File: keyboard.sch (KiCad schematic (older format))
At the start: 37 parts, among them J1 USB_C_Receptacle_USB2.0, J2 -, J3 -, K1 Jumper_NO_Small, P1 SWD, P2 BATT, U1 nRF52810-ND04C, U2 CH554T, U3 TP4057, U4 XC6206P30

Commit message: 更换type-c接口的封装
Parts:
- J1: footprint Connector_USB:USB_C_Receptacle_Amphenol_12401610E4-2A -> Customv2:USB_C_SIMPLE_ONBOARD
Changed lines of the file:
@@
 F 0 "J1" H 1355 6467 50  0000 C CNN
 F 1 "USB_C_Receptacle_USB2.0" H 1355 6376 50  0000 C CNN
-F 2 "Connector_USB:USB_C_Receptacle_Amphenol_12401610E4-2A" H 1400 5600 50  0001 C CNN
+F 2 "Customv2:USB_C_SIMPLE_ONBOARD" H 1400 5600 50  0001 C CNN
 F 3 "https://www.usb.org/sites/default/files/documents/usb_type-c.zip" H 1400 5600 50  0001 C CNN
 	1    1250 5600

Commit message: 增加电容，更改type-c封装为非沉板式
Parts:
- added C9: 1uF, Capacitor_SMD:C_0805_2012Metric, symbol Device:C_Small
- J1: footprint Customv2:USB_C_SIMPLE_ONBOARD -> Customv2:USB_C_SIMPLE
- RL1, RL2, RL3: value 4.7K -> 300
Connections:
- wire segments 111 -> 115
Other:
- moved on the sheet: C5, C6, U4
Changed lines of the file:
@@
 	1    0    0    -1
 $EndComp
-Text GLabel 8800 4300 2    60   Input ~ 0
+Text GLabel 9100 4300 2    60   Input ~ 0
 BATT
-Text GLabel 10500 3700 0    60   Input ~ 0
+Text GLabel 10200 3700 0    60   Input ~ 0
 BATT
 Text GLabel 1500 4500 2    60   Input ~ 0
@@
 L Device:C_Small C5
 U 1 1 58689C6E
-P 7900 5750
-F 0 "C5" H 7910 5820 50  0000 L CNN
-F 1 "1uF" H 7910 5670 50  0000 L CNN
-F 2 "Capacitor_SMD:C_0805_2012Metric" H 7900 5750 50  0001 C CNN
-F 3 "" H 7900 5750 50  0000 C CNN
-	1    7900 5750
+P 9000 4450
+F 0 "C5" H 9010 4520 50  0000 L CNN
+F 1 "1uF" H 9010 4370 50  0000 L CNN
+F 2 "Capacitor_SMD:C_0805_2012Metric" H 9000 4450 50  0001 C CNN
+F 3 "" H 9000 4450 50  0000 C CNN
+	1    9000 4450
 	1    0    0    -1
 $EndComp
@@
 L Device:C_Small C6
 U 1 1 58689C99
-P 8100 5750
-F 0 "C6" H 8110 5820 50  0000 L CNN
-F 1 "1uF" H 8110 5670 50  0000 L CNN
-F 2 "Capacitor_SMD:C_0805_2012Metric" H 8100 5750 50  0001 C CNN
-F 3 "" H 8100 5750 50  0000 C CNN
-	1    8100 5750
-	1    0    0    -1
-$EndComp
-Text GLabel 7900 5650 1    60   Input ~ 0
-BATT
-Text GLabel 8100 5650 1    60   Input ~ 0
-3V3
-$Comp
-L keyboard-rescue:GND-RESCUE-ble4100-nrf-ble4100-nrf-rescue #PWR012
-U 1 1 5868A56A
-P 8000 5950
-F 0 "#PWR012" H 8000 5700 50  0001 C CNN
-F 1 "GND" H 8000 5800 50  0000 C CNN
-F 2 "" H 8000 5950 50  0000 C CNN
-F 3 "" H 8000 5950 50  0000 C CNN
-	1    8000 5950
+P 10500 4950
+F 0 "C6" H 10510 5020 50  0000 L CNN
+F 1 "1uF" H 10510 4870 50  0000 L CNN
+F 2 "Capacitor_SMD:C_0805_2012Metric" H 10500 4950 50  0001 C CNN
+F 3 "" H 10500 4950 50  0000 C CNN
+	1    10500 4950
 	1    0    0    -1
 $EndComp
@@
 Wire Notes Line
 	7300 6300 11200 6300
-Wire Wire Line
-	7900 5850 7900 5900
-Wire Wire Line
-	7900 5900 8000 5900
-Wire Wire Line
-	8100 5900 8100 5850
-Wire Wire Line
-	8000 5900 8000 5950
-Connection ~ 8000 5900
 $Comp
 L keyboard-rescue:CH554T-ch554t U2
@@
 Wire Wire Line
 	8700 5600 8950 5600
-Wire Wire Line
-	8000 5900 8100 5900
 Wire Wire Line
 	3650 6200 4050 6200
@@
 L Regulator_Linear:AP2127N-3.0 U4
 U 1 1 5AE6D677
-P 10250 4750
-F 0 "U4" H 10250 4992 50  0000 C CNN
-F 1 "XC6206P30" H 10250 4901 50  0000 C CNN
-F 2 "Package_TO_SOT_SMD:SOT-23" H 10250 4975 50  0001 C CIN
-F 3 "https://www.diodes.com/assets/Datasheets/AP2127.pdf" H 10250 4750 50  0001 C CNN
-	1    10250 4750
-	1    0    0    -1
-$EndComp
-Text GLabel 9950 4750 0    60   Input ~ 0
+P 10100 4750
+F 0 "U4" H 10100 4992 50  0000 C CNN
+F 1 "XC6206P30" H 10100 4901 50  0000 C CNN
+F 2 "Package_TO_SOT_SMD:SOT-23" H 10100 4975 50  0001 C CIN
+F 3 "https://www.diodes.com/assets/Datasheets/AP2127.pdf" H 10100 4750 50  0001 C CNN
+	1    10100 4750
+	1    0    0    -1
+$EndComp
+Text GLabel 9800 4750 0    60   Input ~ 0
 BATT
-Text GLabel 10550 4750 2    60   Input ~ 0
+Text GLabel 10600 4750 2    60   Input ~ 0
 3V3
 $Comp
 L keyboard-rescue:GND-RESCUE-ble4100-nrf-ble4100-nrf-rescue #PWR016
 U 1 1 5AE6D8BF
-P 10250 5050
-F 0 "#PWR016" H 10250 4800 50  0001 C CNN
-F 1 "GND" H 10250 4900 50  0000 C CNN
-F 2 "" H 10250 5050 50  0000 C CNN
-F 3 "" H 10250 5050 50  0000 C CNN
-	1    10250 5050
+P 10100 5050
+F 0 "#PWR016" H 10100 4800 50  0001 C CNN
+F 1 "GND" H 10100 4900 50  0000 C CNN
+F 2 "" H 10100 5050 50  0000 C CNN
+F 3 "" H 10100 5050 50  0000 C CNN
+	1    10100 5050
 	1    0    0    -1
 $EndComp
@@
 F 0 "J1" H 1355 6467 50  0000 C CNN
 F 1 "USB_C_Receptacle_USB2.0" H 1355 6376 50  0000 C CNN
-F 2 "Customv2:USB_C_SIMPLE_ONBOARD" H 1400 5600 50  0001 C CNN
+F 2 "Customv2:USB_C_SIMPLE" H 1400 5600 50  0001 C CNN
 F 3 "https://www.usb.org/sites/default/files/documents/usb_type-c.zip" H 1400 5600 50  0001 C CNN
 	1    1250 5600
@@
 P 5550 4450
 F 0 "RL1" H 5580 4470 50  0000 L CNN
-F 1 "4.7K" H 5580 4410 50  0000 L CNN
+F 1 "300" H 5580 4410 50  0000 L CNN
 F 2 "Resistor_SMD:R_0805_2012Metric" H 5550 4450 50  0001 C CNN
 F 3 "" H 5550 4450 50  0000 C CNN
@@
 P 5550 4750
 F 0 "RL2" H 5580 4770 50  0000 L CNN
-F 1 "4.7K" H 5580 4710 50  0000 L CNN
+F 1 "300" H 5580 4710 50  0000 L CNN
 F 2 "Resistor_SMD:R_0805_2012Metric" H 5550 4750 50  0001 C CNN
 F 3 "" H 5550 4750 50  0000 C CNN
@@
 P 5550 5050
 F 0 "RL3" H 5580 5070 50  0000 L CNN
-F 1 "4.7K" H 5580 5010 50  0000 L CNN
+F 1 "300" H 5580 5010 50  0000 L CNN
 F 2 "Resistor_SMD:R_0805_2012Metric" H 5550 5050 50  0001 C CNN
 F 3 "" H 5550 5050 50  0000 C CNN
@@
 Wire Bus Line
 	3850 1250 5050 1250
-Connection ~ 3850 1250
 Text Label 5050 7050 0    50   ~ 0
 BUS_A
@@
 Text Notes 7750 4850 0    50   ~ 0
 I_{chrg} = 1000/R2
+$Comp
+L keyboard-rescue:GND-RESCUE-ble4100-nrf-ble4100-nrf-rescue #PWR023
+U 1 1 5CC46D5E
+P 10500 5050
+F 0 "#PWR023" H 10500 4800 50  0001 C CNN
+F 1 "GND" H 10500 4900 50  0000 C CNN
+F 2 "" H 10500 5050 50  0000 C CNN
+F 3 "" H 10500 5050 50  0000 C CNN
+	1    10500 5050
+	1    0    0    -1
+$EndComp
+Wire Wire Line
+	10400 4750 10500 4750
+Wire Wire Line
+	10500 4850 10500 4750
+Connection ~ 10500 4750
+Wire Wire Line
+	10500 4750 10600 4750
 Wire Bus Line
-	2100 1250 3850 1250
+	5050 1250 5050 1500
 Wire Bus Line
-	2200 3150 3850 3150
+	3850 1250 3850 1900
 Wire Bus Line
-	3850 1250 3850 3150
+	2200 3150 2300 3150
 Wire Bus Line
-	5050 1250 5050 7050
+	2100 1250 2200 1250
+Wire Wire Line
+	8800 4300 9000 4300
+Wire Wire Line
+	9000 4350 9000 4300
+Connection ~ 9000 4300
+Wire Wire Line
+	9000 4300 9100 4300
+$Comp
+L keyboard-rescue:GND-RESCUE-ble4100-nrf-ble4100-nrf-rescue #PWR022
+U 1 1 5CCD94C3
+P 9000 4550
+F 0 "#PWR022" H 9000 4300 50  0001 C CNN
+F 1 "GND" H 9000 4400 50  0000 C CNN
+F 2 "" H 9000 4550 50  0000 C CNN
+F 3 "" H 9000 4550 50  0000 C CNN
+	1    9000 4550
+	1    0    0    -1
+$EndComp
+Wire Wire Line
+	10500 3700 10300 3700
+$Comp
+L Device:C_Small C9
+U 1 1 5CD13C66
+P 10300 3900
+F 0 "C9" H 10310 3970 50  0000 L CNN
+F 1 "1uF" H 10310 3820 50  0000 L CNN
+F 2 "Capacitor_SMD:C_0805_2012Metric" H 10300 3900 50  0001 C CNN
+F 3 "" H 10300 3900 50  0000 C CNN
+	1    10300 3900
+	1    0    0    -1
+$EndComp
+Wire Wire Line
+	10300 3800 10300 3700
+Connection ~ 10300 3700
+Wire Wire Line
+	10300 3700 10200 3700
+$Comp
+L keyboard-rescue:GND-RESCUE-ble4100-nrf-ble4100-nrf-rescue #PWR012
+U 1 1 5CD4AD12
+P 10300 4000
+F 0 "#PWR012" H 10300 3750 50  0001 C CNN
+F 1 "GND" H 10300 3850 50  0000 C CNN
+F 2 "" H 10300 4000 50  0000 C CNN
+F 3 "" H 10300 4000 50  0000 C CNN
+	1    10300 4000
+	1    0    0    -1
+$EndComp
 $EndSCHEMATC

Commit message: 增加RGB LED
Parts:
- added D25: LED_CRGB, LED_SMD:LED_RGB_1210, symbol Device:LED_RABG
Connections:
- wire segments 115 -> 124
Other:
- moved on the sheet: J2, J3, JP1, LED1, LED2, LED3, RL1, RL2, RL3

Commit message: 添加一些文字说明
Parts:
- J1: symbol keyboard-rescue:USB_C_Receptacle_USB2.0-Connector -> Connector:USB_C_Receptacle_USB2.0
- K1: value Jumper_NO_Small -> SW; symbol keyboard-rescue:Jumper_NO_Small-RESCUE-ble4100-nrf-ble4100-nrf-rescue -> Switch:SW_Push
- P1: symbol keyboard-rescue:CONN_01X04-RESCUE-ble4100-nrf-ble4100-nrf-rescue -> Connector_Generic:Conn_01x04
- P2: symbol keyboard-rescue:CONN_01X02-RESCUE-ble4100-nrf-ble4100-nrf-rescue -> Connector_Generic:Conn_01x02
- U3: symbol keyboard-rescue:TP4057-RESCUE-ble4100-nrf-ble4100-nrf-rescue -> custom:TP4057
- renumbered LED1 to D101, LED2 to D102, LED3 to D103, D25 to D104, RL1 to R101, RL2 to R102, RL3 to R103
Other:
- note added: "K1 start download,\nplace near to UDP line."
- note added: "Please check your \nLED pinset carefully."
- note removed: "Key to start download, place near to UDP line."

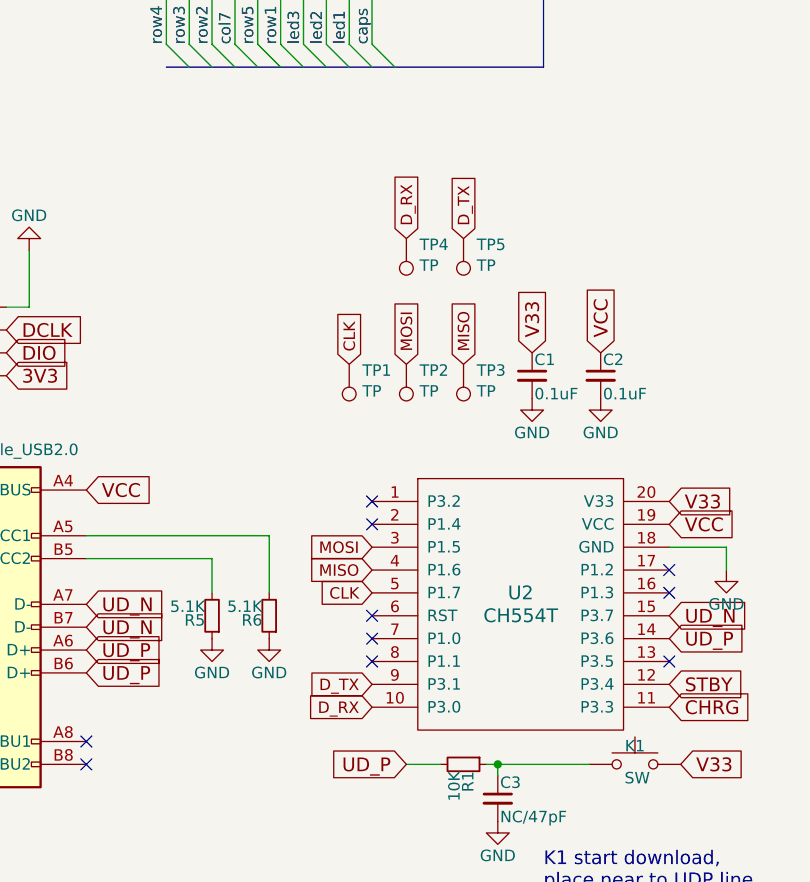
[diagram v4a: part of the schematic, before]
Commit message: 修改USB部分的部分线路布局
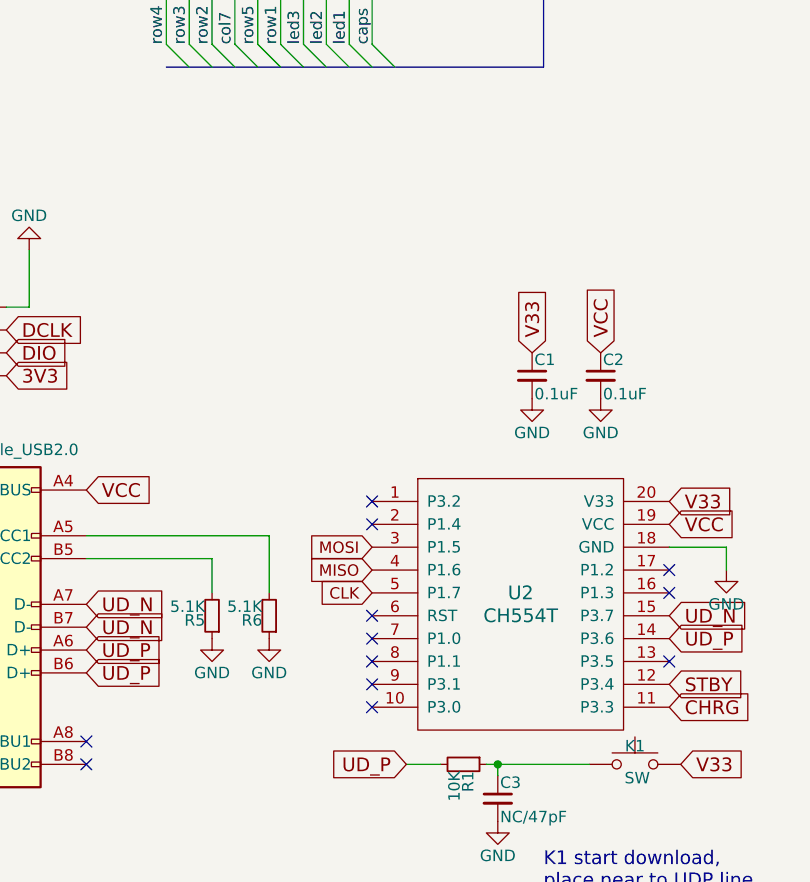
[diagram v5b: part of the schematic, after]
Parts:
- removed TP1, TP2, TP3, TP4, TP5: TP, TestPoint:TestPoint_Pad_D1.0mm, symbol Connector:TestPoint
- K1: footprint Resistor_SMD:R_0805_2012Metric -> Button_Switch_SMD:SW_SPST_TL3342
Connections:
- net D_RX: no longer names the net of U2.10 (P3.0)
- net D_TX: no longer names the net of U2.9 (P3.1)
- no-connect marks 10 -> 12
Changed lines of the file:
@@
 F 0 "K1" H 4250 6280 50  0000 C CNN
 F 1 "SW" H 4260 6140 50  0000 C CNN
-F 2 "Resistor_SMD:R_0805_2012Metric" H 4250 6200 50  0001 C CNN
+F 2 "Button_Switch_SMD:SW_SPST_TL3342" H 4250 6200 50  0001 C CNN
 F 3 "" H 4250 6200 50  0001 C CNN
 	1    4250 6200
@@
 Wire Wire Line
 	2650 5200 2650 5450
-$Comp
-L Connector:TestPoint TP2
-U 1 1 5C5EBA1D
-P 3250 4450
-F 0 "TP2" H 3192 4477 50  0000 R CNN
-F 1 "TP" H 3192 4568 50  0000 R CNN
-F 2 "TestPoint:TestPoint_Pad_D1.0mm" H 3450 4450 50  0001 C CNN
-F 3 "~" H 3450 4450 50  0001 C CNN
-	1    3250 4450
-	-1   0    0    1
-$EndComp
-$Comp
-L Connector:TestPoint TP3
-U 1 1 5C5EBB78
-P 3500 4450
-F 0 "TP3" H 3442 4477 50  0000 R CNN
-F 1 "TP" H 3442 4568 50  0000 R CNN
-F 2 "TestPoint:TestPoint_Pad_D1.0mm" H 3700 4450 50  0001 C CNN
-F 3 "~" H 3700 4450 50  0001 C CNN
-	1    3500 4450
-	-1   0    0    1
-$EndComp
 Text GLabel 3450 2300 2    50   Input ~ 0
 CLK
 Text GLabel 3100 5450 0    50   Input ~ 0
 CLK
-$Comp
-L Connector:TestPoint TP1
-U 1 1 5C63C828
-P 3000 4450
-F 0 "TP1" H 2942 4477 50  0000 R CNN
-F 1 "TP" H 2942 4568 50  0000 R CNN
-F 2 "TestPoint:TestPoint_Pad_D1.0mm" H 3200 4450 50  0001 C CNN
-F 3 "~" H 3200 4450 50  0001 C CNN
-	1    3000 4450
-	-1   0    0    1
-$EndComp
 $Comp
 L Device:C_Small C8
@@
 Wire Wire Line
 	2200 1400 2150 1400
-Text GLabel 3100 5850 0    50   Input ~ 0
-D_TX
-Text GLabel 3100 5950 0    50   Input ~ 0
-D_RX
-Text GLabel 3500 3900 1    50   Input ~ 0
-D_TX
-Text GLabel 3250 3900 1    50   Input ~ 0
-D_RX
-$Comp
-L Connector:TestPoint TP5
-U 1 1 5CE90B6C
-P 3500 3900
-F 0 "TP5" H 3442 3927 50  0000 R CNN
-F 1 "TP" H 3442 4018 50  0000 R CNN
-F 2 "TestPoint:TestPoint_Pad_D1.0mm" H 3700 3900 50  0001 C CNN
-F 3 "~" H 3700 3900 50  0001 C CNN
-	1    3500 3900
-	-1   0    0    1
-$EndComp
-$Comp
-L Connector:TestPoint TP4
-U 1 1 5CEC40AA
-P 3250 3900
-F 0 "TP4" H 3192 3927 50  0000 R CNN
-F 1 "TP" H 3192 4018 50  0000 R CNN
-F 2 "TestPoint:TestPoint_Pad_D1.0mm" H 3450 3900 50  0001 C CNN
-F 3 "~" H 3450 3900 50  0001 C CNN
-	1    3250 3900
-	-1   0    0    1
-$EndComp
 NoConn ~ 3100 5150
 NoConn ~ 3100 5650
@@
 	1    0    0    -1
 $EndComp
-Text GLabel 3500 4450 1    50   Input ~ 0
-MISO
 Text GLabel 3100 5350 0    50   Input ~ 0
 MISO
 Text GLabel 3100 5250 0    50   Input ~ 0
 MOSI
-Text GLabel 3250 4450 1    50   Input ~ 0
-MOSI
-Text GLabel 3000 4450 1    50   Input ~ 0
-CLK
 Wire Bus Line
 	3850 1250 5050 1250
@@
 Please check your \nLED pinset carefully.
 Connection ~ 3850 1250
+NoConn ~ 3100 5850
+NoConn ~ 3100 5950
 Wire Bus Line
 	2100 1250 3850 1250

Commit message: Rev.E
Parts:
- removed C3: NC/47pF, Capacitor_SMD:C_0805_2012Metric, symbol Device:C_Small
- removed JP1: Jumper, Jumper:SolderJumper-2_P1.3mm_Bridged2Bar_Pad1.0x1.5mm, symbol Jumper:SolderJumper_2_Bridged
- added K2: SW, Button_Switch_SMD:SW_SPST_TL3342, symbol Switch:SW_Push
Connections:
- net GND: now also K2.2
- net GPIO0: now also J3.4 (Pin_4); no longer J3.2 (Pin_2)
- net GPIO2: now also J3.2 (Pin_2), U1.3 (P21/RESET), K2.1; no longer J3.4 (Pin_4), U1.32 (P19)
- net caps: now also U1.32 (P19); no longer U1.3 (P21/RESET)
- net CLK renamed UART_TX
- net MISO renamed UART_RX
- net MOSI: no longer names the net of U2.3 (P1.5)
- no-connect marks 12 -> 13
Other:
- note added: "Press K1 to let CH552 enter download mode.\nPlace K1 near to UDP line."
- note removed: "K1 start download,\nplace near to UDP line."
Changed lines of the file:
@@
 encoding utf-8
 Sheet 1 2
-Title "ukbdc - schematic"
-Date "17 jul 2013"
+Title "Lot60-BLE - schematic"
+Date "2019-08-15"
 Rev ""
-Comp "komar"
+Comp "Lotlab"
 Comment1 ""
 Comment2 ""
@@
 	0    1    1    0
 $EndComp
-$Comp
-L Device:C_Small C3
-U 1 1 5A0DBAA2
-P 3650 6350
-F 0 "C3" H 3660 6420 50  0000 L CNN
-F 1 "NC/47pF" H 3660 6270 50  0000 L CNN
-F 2 "Capacitor_SMD:C_0805_2012Metric" H 3650 6350 50  0001 C CNN
-F 3 "~" H 3650 6350 50  0000 C CNN
-	1    3650 6350
-	1    0    0    -1
-$EndComp
 Text GLabel 3250 6200 0    60   Input ~ 0
 UD_P
 Wire Wire Line
 	3250 6200 3400 6200
-Wire Wire Line
-	3600 6200 3650 6200
-Wire Wire Line
-	3650 6250 3650 6200
-Connection ~ 3650 6200
-$Comp
-L power:GND #PWR07
-U 1 1 5A0DBD78
-P 3650 6450
-F 0 "#PWR07" H 3650 6200 50  0001 C CNN
-F 1 "GND" H 3650 6300 50  0000 C CNN
-F 2 "" H 3650 6450 50  0001 C CNN
-F 3 "" H 3650 6450 50  0001 C CNN
-	1    3650 6450
-	1    0    0    -1
-$EndComp
 $Comp
 L Switch:SW_Push K1
@@
 	1    0    0    -1
 $EndComp
-Text Notes 3850 6750 0    60   ~ 0
-K1 start download,\nplace near to UDP line.
+Text Notes 2750 6600 0    60   ~ 0
+Press K1 to let CH552 enter download mode.\nPlace K1 near to UDP line.
 Wire Wire Line
 	8950 5600 8950 5650
 Wire Wire Line
 	8700 5600 8950 5600
-Wire Wire Line
-	3650 6200 4050 6200
 Entry Wire Line
 	2500 3050 2600 3150
@@
 Text Label 2900 1550 1    50   ~ 0
 col14
-Text Label 3100 3050 1    50   ~ 0
+Text Label 3450 2500 0    50   ~ 0
 caps
 Text Label 3000 3050 1    50   ~ 0
@@
 	2650 5200 2650 5450
 Text GLabel 3450 2300 2    50   Input ~ 0
-CLK
+UART_TX
 Text GLabel 3100 5450 0    50   Input ~ 0
-CLK
+UART_TX
 $Comp
 L Device:C_Small C8
@@
 Text Label 3450 2600 0    50   ~ 0
 GPIO1
-Text Label 3450 2500 0    50   ~ 0
-GPIO2
 Wire Wire Line
 	2800 2850 2800 3050
@@
 Entry Wire Line
 	2800 3050 2900 3150
-Entry Wire Line
-	5050 6650 5150 6750
-Wire Wire Line
-	5150 6750 5400 6750
-Text Label 5150 6750 0    50   ~ 0
-GPIO2
-$Comp
-L Jumper:SolderJumper_2_Bridged JP1
-U 1 1 5D27A02A
-P 5550 6750
-F 0 "JP1" H 5550 6950 50  0000 C CNN
-F 1 "Jumper" H 5550 6850 50  0000 C CNN
-F 2 "Jumper:SolderJumper-2_P1.3mm_Bridged2Bar_Pad1.0x1.5mm" H 5550 6750 50  0001 C CNN
-F 3 "~" H 5550 6750 50  0001 C CNN
-	1    5550 6750
-	-1   0    0    1
-$EndComp
-Text GLabel 5700 6750 2    50   Input ~ 0
-MOSI
 Text GLabel 3450 2400 2    50   Input ~ 0
-MISO
+UART_RX
 Entry Wire Line
 	5050 7050 5150 7150
@@
 Wire Wire Line
 	5150 7350 5400 7350
-Text Label 5150 7350 0    50   ~ 0
+Text Label 5150 7150 0    50   ~ 0
 GPIO2
 Text Label 5150 7250 0    50   ~ 0
 GPIO1
-Text Label 5150 7150 0    50   ~ 0
+Text Label 5150 7350 0    50   ~ 0
 GPIO0
 $Comp
@@
 $EndComp
 Text GLabel 3100 5350 0    50   Input ~ 0
-MISO
-Text GLabel 3100 5250 0    50   Input ~ 0
-MOSI
+UART_RX
 Wire Bus Line
 	3850 1250 5050 1250
@@
 NoConn ~ 3100 5850
 NoConn ~ 3100 5950
+NoConn ~ 3100 5250
+Wire Wire Line
+	3600 6200 4050 6200
+Text Label 3100 3050 1    50   ~ 0
+GPIO2
+Entry Wire Line
+	5050 6700 5150 6800
+Text Label 5150 6800 0    50   ~ 0
+GPIO2
+Wire Wire Line
+	5150 6800 5400 6800
 Wire Bus Line
 	2100 1250 3850 1250
@@
 Wire Bus Line
 	5050 1250 5050 7650
+$Comp
+L Switch:SW_Push K2
+U 1 1 5D5B2681
+P 5600 6800
+F 0 "K2" H 5600 6880 50  0000 C CNN
+F 1 "SW" H 5610 6740 50  0000 C CNN
+F 2 "Button_Switch_SMD:SW_SPST_TL3342" H 5600 6800 50  0001 C CNN
+F 3 "" H 5600 6800 50  0001 C CNN
+	1    5600 6800
+	1    0    0    -1
+$EndComp
+$Comp
+L power:GND #PWR07
+U 1 1 5D5B2ED7
+P 5800 6800
+F 0 "#PWR07" H 5800 6550 50  0001 C CNN
+F 1 "GND" H 5805 6627 50  0000 C CNN
+F 2 "" H 5800 6800 50  0001 C CNN
+F 3 "" H 5800 6800 50  0001 C CNN
+	1    5800 6800
+	0    -1   -1   0
+$EndComp
 $EndSCHEMATC

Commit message: 增加顶部电池P2.0接口，修改LED为RGBA封装，避免优信店内LED需要反装的问题。微调LOGO位置
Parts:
- added P3: BATT, Connector_PinSocket_2.00mm:PinSocket_1x02_P2.00mm_Vertical, symbol Connector_Generic:Conn_01x02
- D104: value LED_CRGB -> FM-3528RGBA; symbol Device:LED_RABG -> Device:LED_RGBA
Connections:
- net 3V3: now also D104.4 (A); no longer D104.2 (A)
- net BATT: now also P3.1 (Pin_1)
- net GND: now also P3.2 (Pin_2)
- net at D102.2 (A), R102.1: now also D104.2 (GK); no longer D104.4 (GK)
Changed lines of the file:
@@
 EESchema Schematic File Version 4
 LIBS:keyboard-cache
-EELAYER 29 0
+EELAYER 30 0
 EELAYER END
 $Descr A4 11693 8268
@@
 $EndComp
 $Comp
-L Device:LED_RABG D104
+L Device:LED_RGBA D104
 U 1 1 5CE18492
 P 6100 4600
 F 0 "D104" V 6054 4960 50  0000 L CNN
-F 1 "LED_CRGB" V 6145 4960 50  0000 L CNN
+F 1 "FM-3528RGBA" V 6145 4960 50  0000 L CNN
 F 2 "LED_SMD:LED_RGB_1210" H 6100 4550 50  0001 C CNN
 F 3 "~" H 6100 4550 50  0001 C CNN
@@
 Wire Wire Line
 	5150 6800 5400 6800
-Wire Bus Line
-	2100 1250 3850 1250
-Wire Bus Line
-	3850 1250 3850 3150
-Wire Bus Line
-	2200 3150 3850 3150
-Wire Bus Line
-	5050 1250 5050 7650
 $Comp
 L Switch:SW_Push K2
@@
 	0    -1   -1   0
 $EndComp
+$Comp
+L Connector_Generic:Conn_01x02 P3
+U 1 1 5D6C74C7
+P 10700 3250
+F 0 "P3" H 10700 3400 50  0000 C CNN
+F 1 "BATT" V 10800 3250 50  0000 C CNN
+F 2 "Connector_PinSocket_2.00mm:PinSocket_1x02_P2.00mm_Vertical" H 10700 3250 50  0001 C CNN
+F 3 "" H 10700 3250 50  0000 C CNN
+	1    10700 3250
+	1    0    0    -1
+$EndComp
+Text GLabel 10500 3250 0    60   Input ~ 0
+BATT
+Wire Bus Line
+	5050 1250 5050 7650
+Wire Bus Line
+	2100 1250 3850 1250
+Wire Bus Line
+	3850 1250 3850 3150
+Wire Bus Line
+	2200 3150 3850 3150
+$Comp
+L power:GND #PWR0101
+U 1 1 5D6C7B4E
+P 10500 3350
+F 0 "#PWR0101" H 10500 3100 50  0001 C CNN
+F 1 "GND" H 10500 3200 50  0000 C CNN
+F 2 "" H 10500 3350 50  0000 C CNN
+F 3 "" H 10500 3350 50  0000 C CNN
+	1    10500 3350
+	1    0    0    -1
+$EndComp
 $EndSCHEMATC

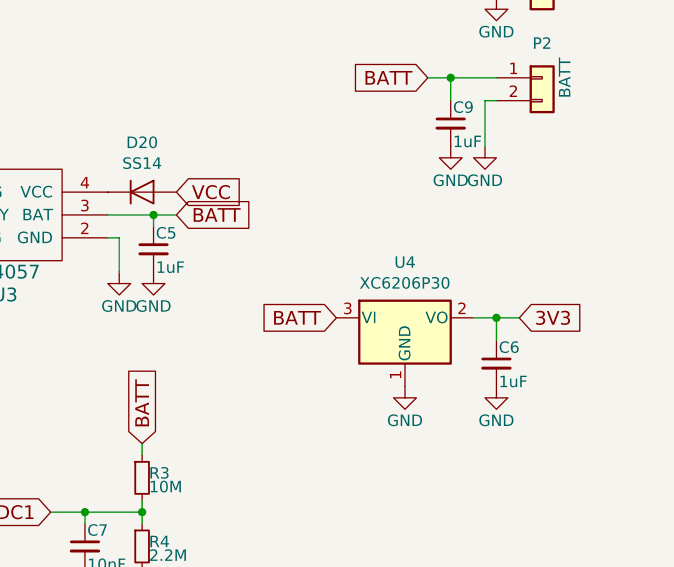
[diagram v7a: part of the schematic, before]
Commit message: 将SS14封装更换为更易买到的SMA，将XC6206P30换为更易买到的XC6206P33
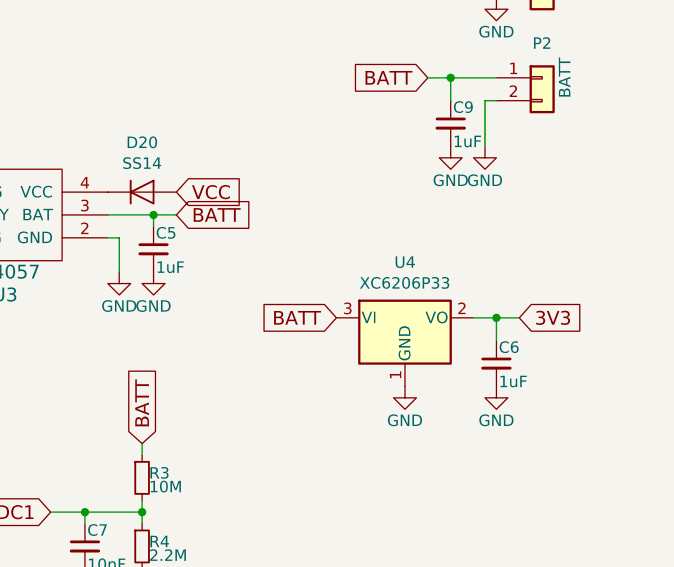
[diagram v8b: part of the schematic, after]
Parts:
- D20: footprint Diode_SMD:D_0805_2012Metric -> Diode_SMD:D_SMA
- U4: value XC6206P30 -> XC6206P33
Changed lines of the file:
@@
 P 10100 4750
 F 0 "U4" H 10100 4992 50  0000 C CNN
-F 1 "XC6206P30" H 10100 4901 50  0000 C CNN
+F 1 "XC6206P33" H 10100 4901 50  0000 C CNN
 F 2 "Package_TO_SOT_SMD:SOT-23" H 10100 4975 50  0001 C CIN
 F 3 "https://www.diodes.com/assets/Datasheets/AP2127.pdf" H 10100 4750 50  0001 C CNN
@@
 F 0 "D20" H 8950 4416 50  0000 C CNN
 F 1 "SS14" H 8950 4325 50  0000 C CNN
-F 2 "Diode_SMD:D_0805_2012Metric" H 8950 4200 50  0001 C CNN
+F 2 "Diode_SMD:D_SMA" H 8950 4200 50  0001 C CNN
 F 3 "~" H 8950 4200 50  0001 C CNN
 	1    8950 4200
